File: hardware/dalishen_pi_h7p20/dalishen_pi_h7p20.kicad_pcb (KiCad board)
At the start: 4 copper layers, 92 x 64 mm, 225 parts, among them J1 Conn_02x05_Odd_Even, J10 RJ45_HR911130A, J1001 USB_C_Receptacle_USB2.0_16P, J2 USB_C_Receptacle_USB2.0_16P, J3 USB_A, J6 5V, J7 OV5640, J9 D500C930SV0, SW1 SW_Push, SW2 SW_Push, SW3 SW_DIP_x03, SW4 SW_Push, SW5 SW_Push, U1 YT8531C, U1001 AIC8800FC, U1002 P25Q80H/P25Q64H/P25Q128HA, U20 USB3343, U3 H7P20N0L128-M3H1, U4 SY7201ABC, U5 XC6206-2.8, U6 EA3036C, U7 P25Q64SH-SSH-IR, U8 XC6206-1.5, U9 CJ3439KDW, X1 NC, Y1 26M, Y1001 26M, 10PPM, Y2 NC

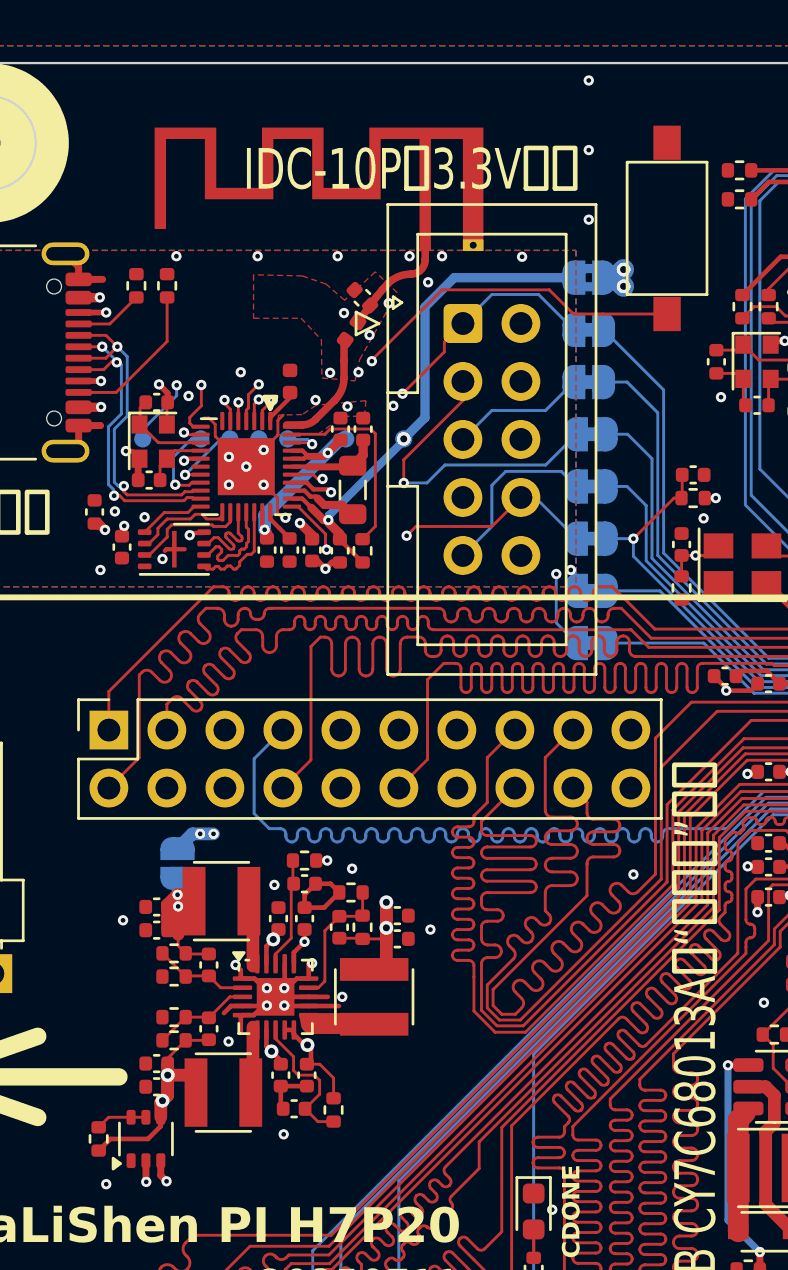
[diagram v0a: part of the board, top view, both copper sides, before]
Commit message: [dalishen_pi_h7p20] 优化LAYOUT
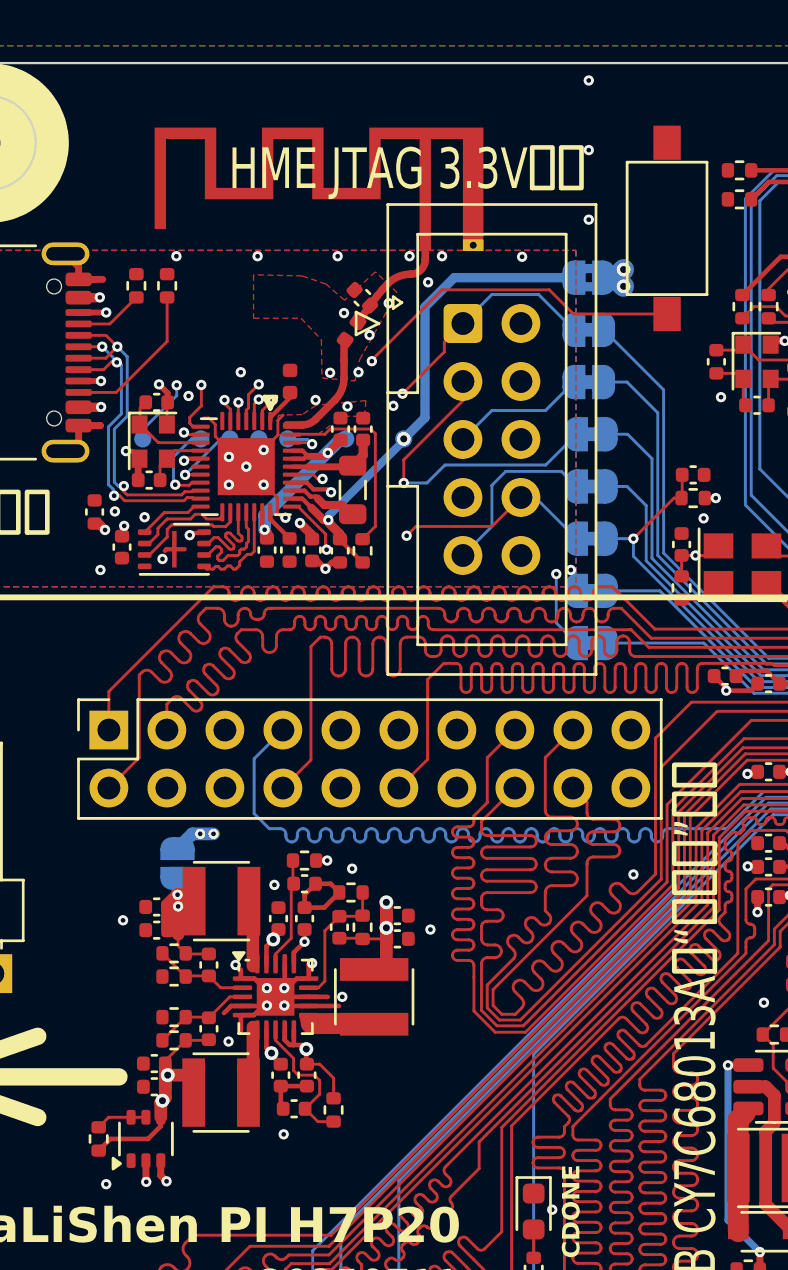
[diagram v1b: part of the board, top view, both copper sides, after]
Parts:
- moved C29 0.10 mm to (119.4, 133.5)
- moved C30 0.10 mm to (119.4, 134.5)
- moved L4 0.10 mm to (122.3, 134.7)
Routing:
- net /VCC_5V: track 195.5 -> 196.4 mm
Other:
- board text added: "HME JTAG 3.3V电平"
- board text removed: "IDC-10P，3.3V电平"

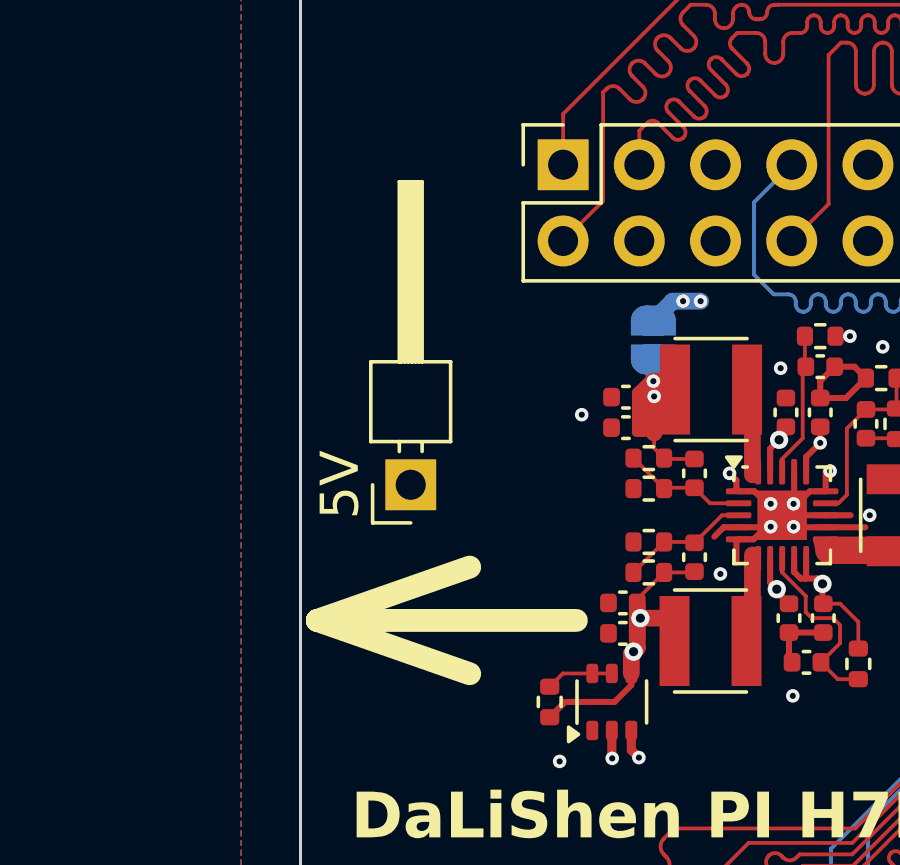
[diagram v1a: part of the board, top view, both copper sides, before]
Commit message: [dalishen_pi_h7p20] 优化LAYOUT
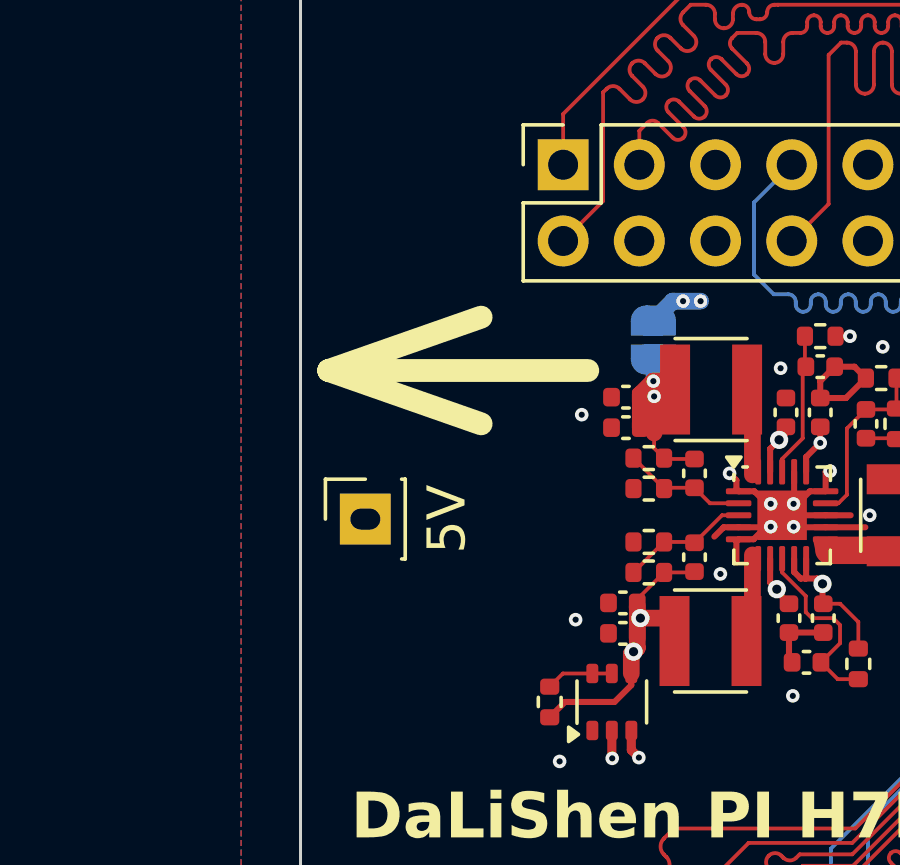
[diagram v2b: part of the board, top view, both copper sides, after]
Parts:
- J6: footprint Connector_PinHeader_2.54mm:PinHeader_1x01_P2.54mm_Horizontal -> Connector_PinSocket_2.54mm:PinSocket_1x01_P2.54mm_Vertical
- moved J6 1.90 mm to (110.8, 130.7)
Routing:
- net /VCC_5V: track 196.4 -> 199.6 mm

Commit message: [dalishen_pi_h7p20] 优化LAYOUT
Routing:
- net /VCC_3V3: track 123.3 -> 124.4 mm
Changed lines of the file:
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@@
 	)
 	(segment
+		(start 180.4924 121.6914)
+		(end 181.991 120.1928)
+		(width 0.5588)
+		(layer "In2.Cu")
+		(net 32)
+	)
+	(segment
 		(start 173.609 125.8824)
 		(end 172.3898 125.8824)
@@
 	)
 	(segment
-		(start 180.4924 121.6914)
-		(end 181.229 120.9548)
-		(width 0.5588)
-		(layer "In2.Cu")
-		(net 32)
-	)
-	(segment
 		(start 175.2346 124.2568)
 		(end 173.609 125.8824)
@@
 		(polygon
 			(pts
-				(xy 165.7858 123.8504) (xy 162.8394 127.0508) (xy 177.7238 129.8448) (xy 181.5846 128.0414) (xy 181.5846 122.9614)
-				(xy 179.832 118.745) (xy 165.7858 118.745)
+				(xy 165.7858 123.8504) (xy 162.8394 127.0508) (xy 177.7238 129.8448) (xy 181.5846 128.0414) (xy 184.658 126.7714)
+				(xy 184.5818 123.444) (xy 182.7784 122.2502) (xy 179.832 118.745) (xy 165.7858 118.745)
 			)
 		)
